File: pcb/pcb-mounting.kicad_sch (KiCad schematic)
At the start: 2 parts

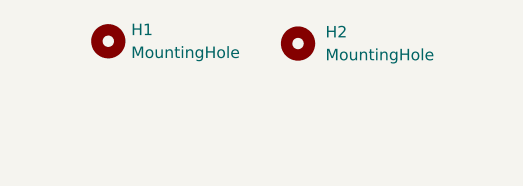
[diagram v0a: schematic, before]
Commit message: ADD new picture, and propper GND plane on top layer
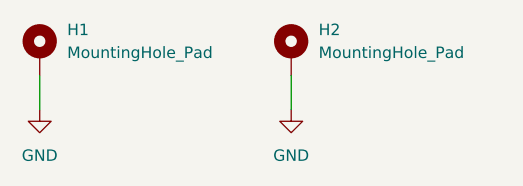
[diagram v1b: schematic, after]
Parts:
- removed H1, H2: MountingHole, MountingHole:MountingHole_3.2mm_M3_DIN965, symbol Mechanical:MountingHole
- added H1, H2: MountingHole_Pad, MountingHole:MountingHole_3.2mm_M3_DIN965_Pad, symbol Mechanical:MountingHole_Pad
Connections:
- new net GND: H1.1, H2.1
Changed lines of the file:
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@@
 (kicad_sch (version 20211123) (generator eeschema)
   (paper "A4")
-  (symbol (lib_id "Mechanical:MountingHole") (at 150.622 91.694 0) (unit 1)
+  (wire (pts (xy 149.86 95.25) (xy 149.86 99.06))
+    (stroke (width 0) (type default) (color 0 0 0 0))
+  )
+  (wire (pts (xy 121.92 95.25) (xy 121.92 99.06))
+    (stroke (width 0) (type default) (color 0 0 0 0))
+  )
+  (symbol (lib_id "power:GND") (at 121.92 99.06 0) (unit 1)
     (in_bom yes) (on_board yes) (fields_autoplaced)
-    (property "Reference" "H2" (id 0) (at 153.67 90.4239 0)
+    (property "Reference" "#PWR0132" (id 0) (at 121.92 105.41 0)
+      (effects (font (size 1.27 1.27)) hide)
+    )
+    (property "Value" "GND" (id 1) (at 121.92 104.14 0))
+    (property "Footprint" "" (id 2) (at 121.92 99.06 0)
+      (effects (font (size 1.27 1.27)) hide)
+    )
+    (property "Datasheet" "" (id 3) (at 121.92 99.06 0)
+      (effects (font (size 1.27 1.27)) hide)
+    )
+    (pin "1")
+  )
+  (symbol (lib_id "Mechanical:MountingHole_Pad") (at 121.92 92.71 0) (unit 1)
+    (in_bom yes) (on_board yes) (fields_autoplaced)
+    (property "Reference" "H1" (id 0) (at 124.968 90.1699 0)
       (effects (font (size 1.27 1.27)) (justify left))
     )
-    (property "Value" "MountingHole" (id 1) (at 153.67 92.9639 0)
+    (property "Value" "MountingHole_Pad" (id 1) (at 124.968 92.7099 0)
       (effects (font (size 1.27 1.27)) (justify left))
     )
-    (property "Footprint" "MountingHole:MountingHole_3.2mm_M3_DIN965" (id 2) (at 150.622 91.694 0)
+    (property "Footprint" "MountingHole:MountingHole_3.2mm_M3_DIN965_Pad" (id 2) (at 121.92 92.71 0)
       (effects (font (size 1.27 1.27)) hide)
     )
-    (property "Datasheet" "~" (id 3) (at 150.622 91.694 0)
+    (property "Datasheet" "~" (id 3) (at 121.92 92.71 0)
       (effects (font (size 1.27 1.27)) hide)
     )
+    (pin "1")
   )
-  (symbol (lib_id "Mechanical:MountingHole") (at 129.54 91.44 0) (unit 1)
+  (symbol (lib_id "Mechanical:MountingHole_Pad") (at 149.86 92.71 0) (unit 1)
     (in_bom yes) (on_board yes) (fields_autoplaced)
-    (property "Reference" "H1" (id 0) (at 132.08 90.1699 0)
+    (property "Reference" "H2" (id 0) (at 152.908 90.1699 0)
       (effects (font (size 1.27 1.27)) (justify left))
     )
-    (property "Value" "MountingHole" (id 1) (at 132.08 92.7099 0)
+    (property "Value" "MountingHole_Pad" (id 1) (at 152.908 92.7099 0)
       (effects (font (size 1.27 1.27)) (justify left))
     )
-    (property "Footprint" "MountingHole:MountingHole_3.2mm_M3_DIN965" (id 2) (at 129.54 91.44 0)
+    (property "Footprint" "MountingHole:MountingHole_3.2mm_M3_DIN965_Pad" (id 2) (at 149.86 92.71 0)
       (effects (font (size 1.27 1.27)) hide)
     )
-    (property "Datasheet" "~" (id 3) (at 129.54 91.44 0)
+    (property "Datasheet" "~" (id 3) (at 149.86 92.71 0)
       (effects (font (size 1.27 1.27)) hide)
     )
+    (pin "1")
+  )
+  (symbol (lib_id "power:GND") (at 149.86 99.06 0) (unit 1)
+    (in_bom yes) (on_board yes) (fields_autoplaced)
+    (property "Reference" "#PWR0133" (id 0) (at 149.86 105.41 0)
+      (effects (font (size 1.27 1.27)) hide)
+    )
+    (property "Value" "GND" (id 1) (at 149.86 104.14 0))
+    (property "Footprint" "" (id 2) (at 149.86 99.06 0)
+      (effects (font (size 1.27 1.27)) hide)
+    )
+    (property "Datasheet" "" (id 3) (at 149.86 99.06 0)
+      (effects (font (size 1.27 1.27)) hide)
+    )
+    (pin "1")
   )
 )

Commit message: REF PCB Layout, Switch to new USB-C Receptable
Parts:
- H1, H2: footprint MountingHole:MountingHole_3.2mm_M3_DIN965_Pad -> MountingHole:MountingHole_2.2mm_M2_Pad
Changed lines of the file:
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@@
       (effects (font (size 1.27 1.27)) (justify left))
     )
-    (property "Footprint" "MountingHole:MountingHole_3.2mm_M3_DIN965_Pad" (id 2) (at 121.92 92.71 0)
+    (property "Footprint" "MountingHole:MountingHole_2.2mm_M2_Pad" (id 2) (at 121.92 92.71 0)
       (effects (font (size 1.27 1.27)) hide)
     )
@@
       (effects (font (size 1.27 1.27)) (justify left))
     )
-    (property "Footprint" "MountingHole:MountingHole_3.2mm_M3_DIN965_Pad" (id 2) (at 149.86 92.71 0)
+    (property "Footprint" "MountingHole:MountingHole_2.2mm_M2_Pad" (id 2) (at 149.86 92.71 0)
       (effects (font (size 1.27 1.27)) hide)
     )
